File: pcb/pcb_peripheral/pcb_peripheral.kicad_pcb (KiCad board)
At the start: 2 copper layers, 46.6 x 42.2 mm, 28 parts, among them J1 Pump 1, J2 Pump 2, J3 Microlab, J4 Sensors, J5 Pump 2, Q1 Q_NMOS_DGS, SW1 Fill, SW2 Pump, SW3 Fill, SW4 Pump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

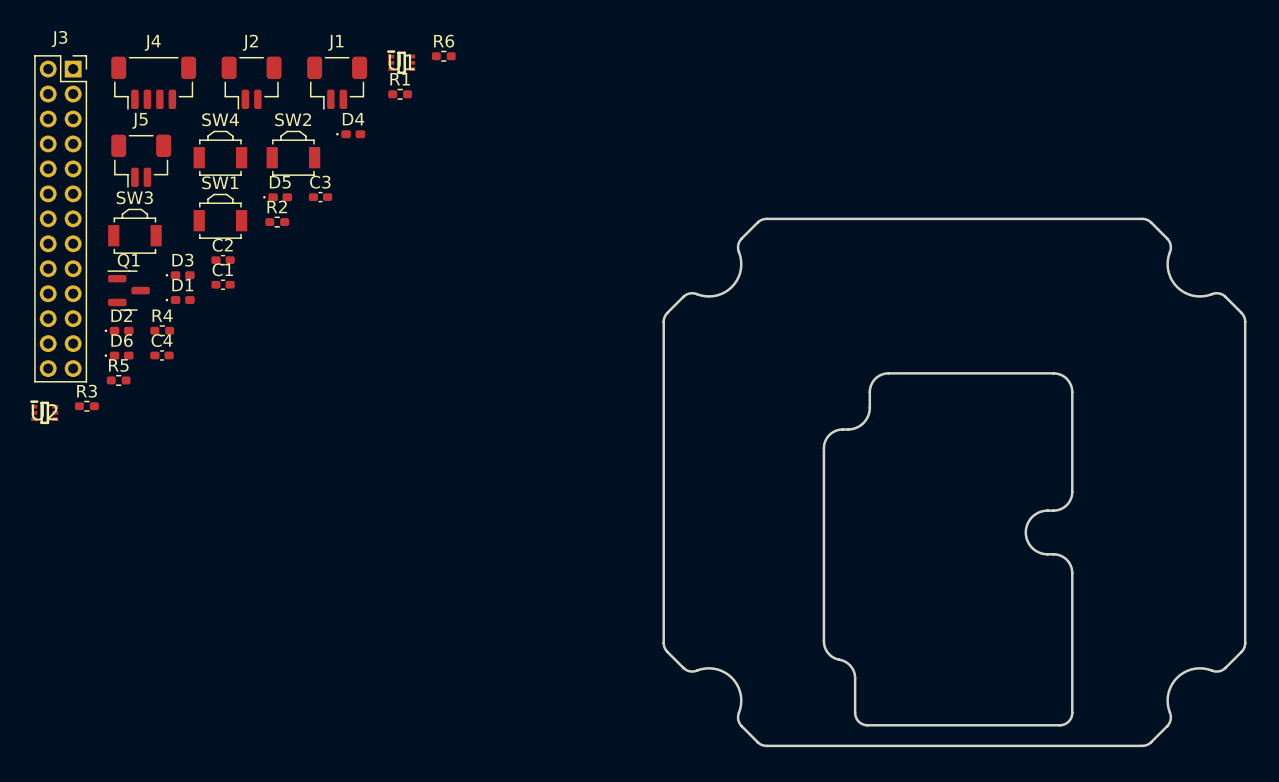
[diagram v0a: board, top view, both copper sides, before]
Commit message: inter-component routing finished
placed and routed all components except IO connections
don't have access to the internet to check the placement of the microlab header therefore no IO routing
might change the placement of the pump, led, and sensor headers when I get internet access
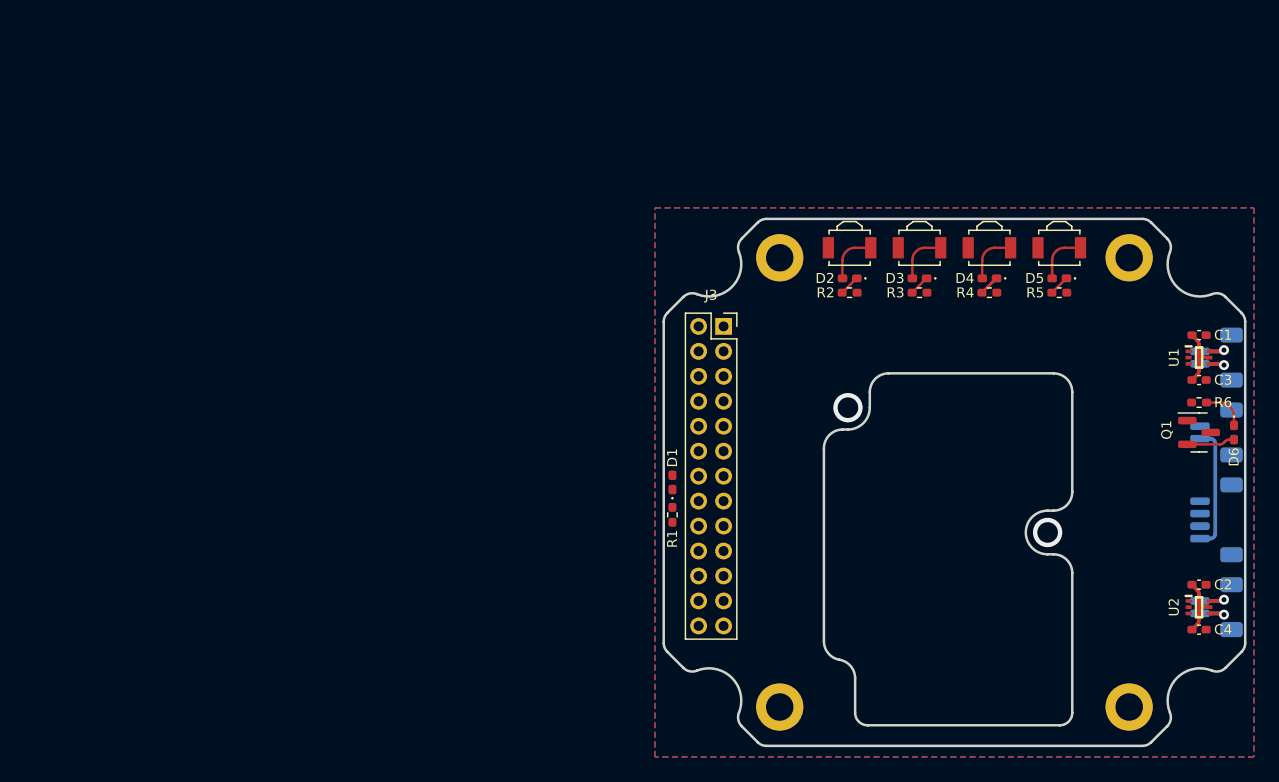
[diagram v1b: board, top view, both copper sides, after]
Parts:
- added H1: M2, MountingHole:MountingHole_2.2mm_M2_DIN965_Pad, F.Cu at (164.0, 82.0)
- added H2: M2, MountingHole:MountingHole_2.2mm_M2_DIN965_Pad, F.Cu at (136.0, 82.0)
- added H3: M2, MountingHole:MountingHole_2.2mm_M2_DIN965_Pad, F.Cu at (136.0, 118.0)
- added H4: M2, MountingHole:MountingHole_2.2mm_M2_DIN965_Pad, F.Cu at (164.0, 118.0)
- J1, J2, J4, J5: moved to B.Cu
- moved U2 93.8 mm to (169.6, 110.0)
- moved J4 92.1 mm to (171.0, 103.0), turned to 90 degrees
- moved D6 89.3 mm to (172.4, 96.0), turned to -90 degrees
- moved J5 88.9 mm to (171.0, 96.0), turned to 90 degrees
- moved J2 88.0 mm to (171.0, 110.0), turned to 90 degrees
- moved Q1 86.5 mm to (169.6, 96.0)
- moved C4 86.0 mm to (169.6, 111.8)
- moved C2 82.4 mm to (169.6, 108.2)
- moved C1 78.3 mm to (169.6, 88.2)
- moved R5 75.7 mm to (158.4, 84.8)
- moved J1 73.8 mm to (171.0, 90.0), turned to 90 degrees
- moved C3 71.9 mm to (169.6, 91.8)
- moved SW3 68.5 mm to (152.8, 81.2)
- moved U1 68.1 mm to (169.6, 90.0)
- moved SW4 67.6 mm to (158.4, 81.2)
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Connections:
- SW2 pad 1: /IO1 -> +5V
- SW2 pad 2: +5V -> /IO1
- SW4 pad 1: /IO3 -> +5V
- SW4 pad 2: +5V -> /IO3
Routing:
- net +5V: track 0.00 -> 20.4 mm
- net /IO1: track 0.00 -> 4.25 mm
- net /IO0: track 0.00 -> 4.25 mm
- net /IO3: track 0.00 -> 4.25 mm
- net /IO2: track 0.00 -> 4.25 mm
- net /IO4: track 0.00 -> 3.86 mm
- net Net-(D6-Pad1): track 0.00 -> 3.50 mm
- net Net-(D4-Pad1): track 0.00 -> 3.28 mm
- net Net-(J1-Pad1): track 0.00 -> 3.17 mm, vias 0 -> 1
- net Net-(J2-Pad2): track 0.00 -> 3.17 mm, vias 0 -> 1
- net Net-(J2-Pad1): track 0.00 -> 3.17 mm, vias 0 -> 1
- net Net-(J1-Pad2): track 0.00 -> 3.17 mm, vias 0 -> 1
- net Net-(D3-Pad1): track 0.00 -> 1.65 mm
- net Net-(D2-Pad1): track 0.00 -> 1.65 mm
- net Net-(D5-Pad1): track 0.00 -> 1.65 mm
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- added copper zone on B.Cu, net GND
- added copper zone on F.Cu, net GND
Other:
- board text added: "LED"
- board text added: "Pump 1"
- board text added: "Pump 2"
- board text added: "Sensors"
